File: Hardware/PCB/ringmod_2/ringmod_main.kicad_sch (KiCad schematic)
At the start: 61 parts, among them J1 Synth_power_2x5, J2 AudioJack2, J3 AudioJack2, J4 AudioJack2, J5 AudioJack2, J9 AudioJack2, U1 NE5532, U2 TL071, U3 TL072

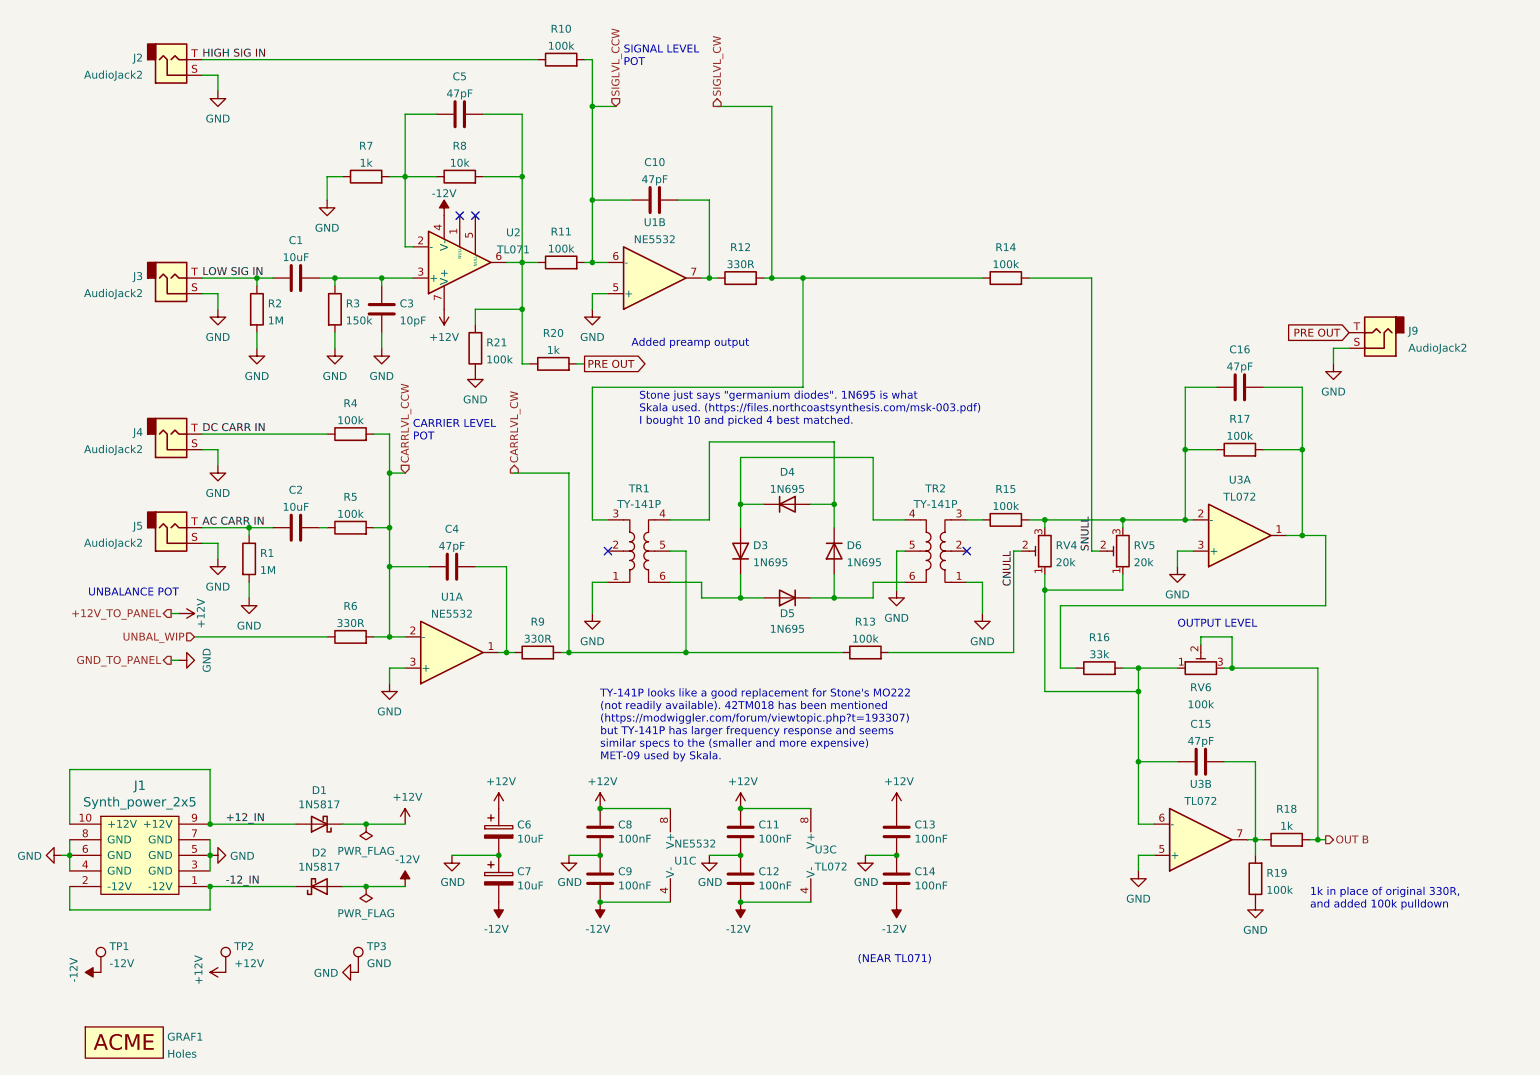
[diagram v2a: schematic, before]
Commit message: remove inst preamp, redesign panel
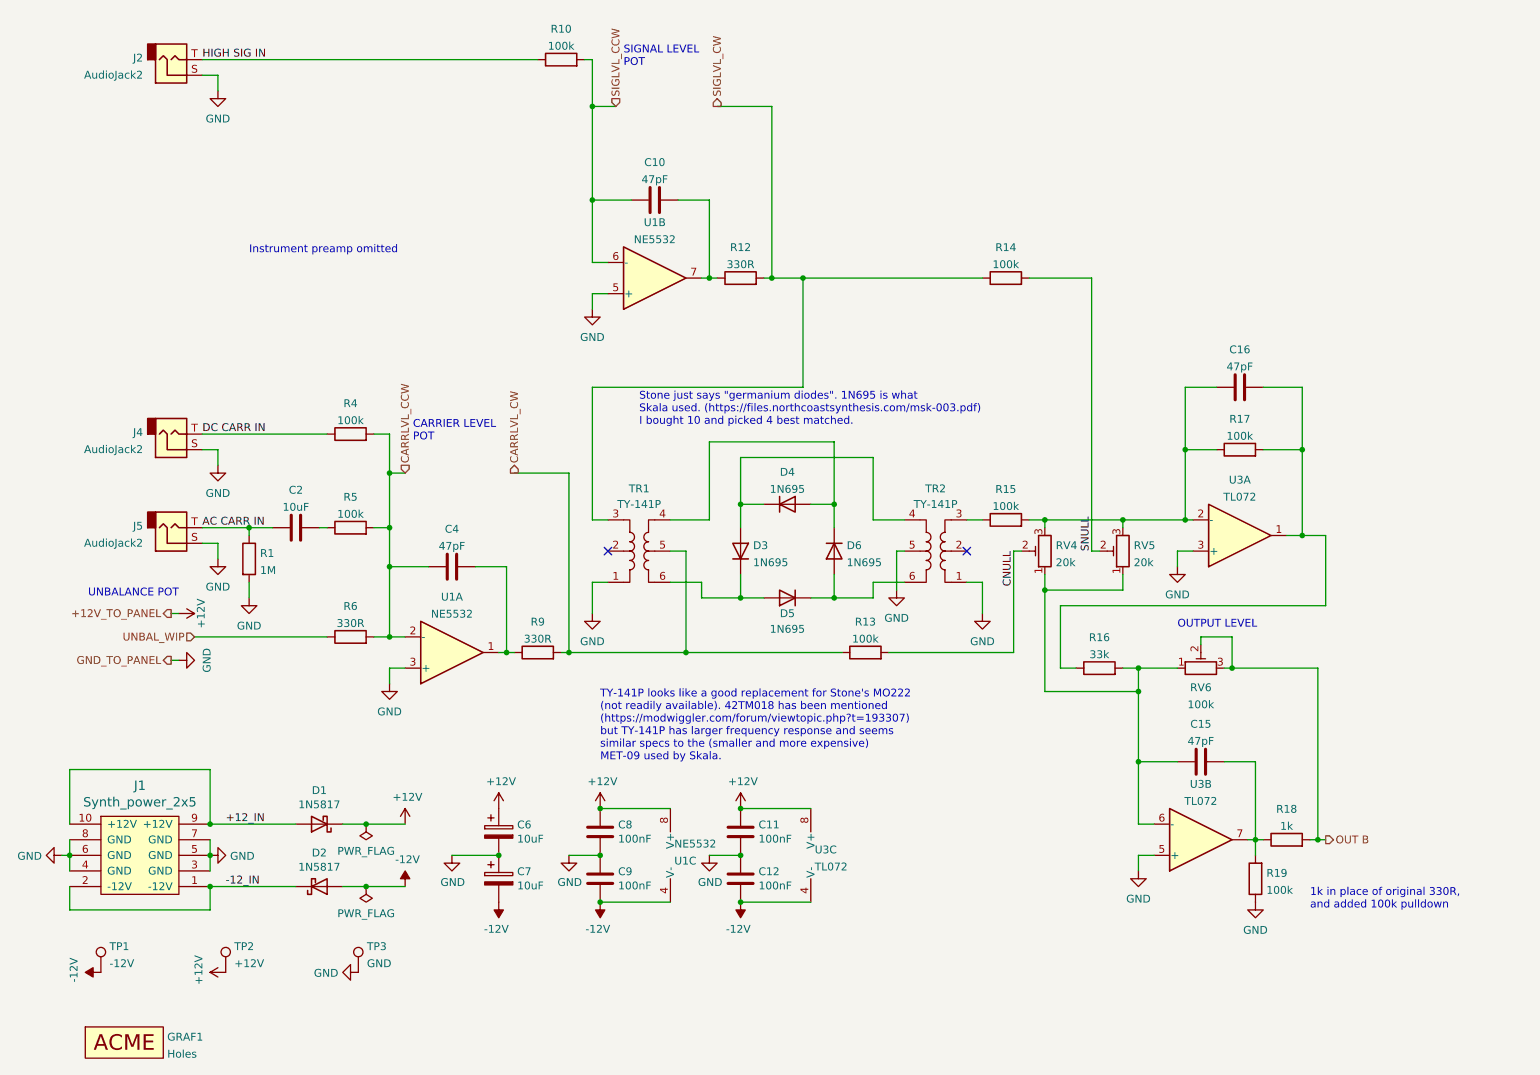
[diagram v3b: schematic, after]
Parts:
- removed C1: 10uF, Capacitor_THT:C_Radial_D6.3mm_H11.0mm_P2.50mm, symbol ao_symbols:C
- removed C13, C14: 100nF, ao_tht:C_Disc_D3.0mm_W1.6mm_P2.50mm, symbol ao_symbols:C
- removed C3: 10pF, ao_tht:C_Disc_D3.0mm_W1.6mm_P2.50mm, symbol ao_symbols:C
- removed C5: 47pF, ao_tht:C_Disc_D3.0mm_W1.6mm_P2.50mm, symbol ao_symbols:C
- removed J3, J9: AudioJack2, ao_tht:Jack_6.35mm_TE-CK-6.35-29B_Horizontal, symbol Connector:AudioJack2
- removed R11, R21: 100k, ao_tht:R_Axial_DIN0207_L6.3mm_D2.5mm_P10.16mm_Horizontal, symbol ao_symbols:R
- removed R2: 1M, ao_tht:R_Axial_DIN0207_L6.3mm_D2.5mm_P10.16mm_Horizontal, symbol ao_symbols:R
- removed R20, R7: 1k, ao_tht:R_Axial_DIN0207_L6.3mm_D2.5mm_P10.16mm_Horizontal, symbol ao_symbols:R
- removed R3: 150k, ao_tht:R_Axial_DIN0207_L6.3mm_D2.5mm_P10.16mm_Horizontal, symbol ao_symbols:R
- removed R8: 10k, ao_tht:R_Axial_DIN0207_L6.3mm_D2.5mm_P10.16mm_Horizontal, symbol ao_symbols:R
- removed U2: TL071, ao_tht:DIP-8_W7.62mm_Socket_LongPads, symbol ao_symbols:TL071
- C2: footprint Capacitor_THT:C_Radial_D6.3mm_H11.0mm_P2.50mm -> ao_tht:C_Radial_D8.0mm_H11.5mm_P3.50mm
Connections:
- no-connect marks 4 -> 2
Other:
- note added: "Instrument preamp omitted"
- note removed: "(NEAR TL071)"
- note removed: "Added preamp output"

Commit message: rm first design; add new holes image
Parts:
- added J10: AudioJack2, ao_tht:Jack_6.35mm_PJ_629HAN_slots, symbol Connector:AudioJack2
- GRAF1: footprint ringmod_panel:ringmod_panel_2_holes -> ringmod:ringmod_panel_2_holes
- J7: renamed from J2; footprint ao_tht:Jack_6.35mm_TE-CK-6.35-29B_Horizontal -> ao_tht:Jack_6.35mm_PJ_629HAN_slots
- J8: renamed from J4; footprint ao_tht:Jack_6.35mm_TE-CK-6.35-29B_Horizontal -> ao_tht:Jack_6.35mm_PJ_629HAN_slots
- J9: renamed from J5; footprint ao_tht:Jack_6.35mm_TE-CK-6.35-29B_Horizontal -> ao_tht:Jack_6.35mm_PJ_629HAN_slots
- renumbered C10 to C1, C9 to C10, C12 to C11, C16 to C2, C2 to C3, C15 to C5, C8 to C7, C11 to C8, C7 to C9, D4 to D1, D3 to D2, D6 to D3, D5 to D4, D1 to D5, D2 to D6, J1 to J11, R10 to R1, R9 to R10, R13 to R11, R16 to R12, R18 to R13, R19 to R14, R12 to R2, R14 to R3, R17 to R5, R15 to R6, R5 to R7, R1 to R8, R6 to R9, RV4 to RV7, RV5 to RV8, RV6 to RV9, U3 to U2
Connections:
- net GND: now also J10.S
- net HIGH SIG IN renamed SIG IN
- net OUT B renamed OUT
- net OUT: now also J10.T
